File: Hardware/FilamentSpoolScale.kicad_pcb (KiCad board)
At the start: 2 copper layers, 62 x 76 mm, 7 parts, among them J1 0.91 inch OLED, J2 Load Cell, J3 Screw_Terminal_01x02, SW1 SW_Push

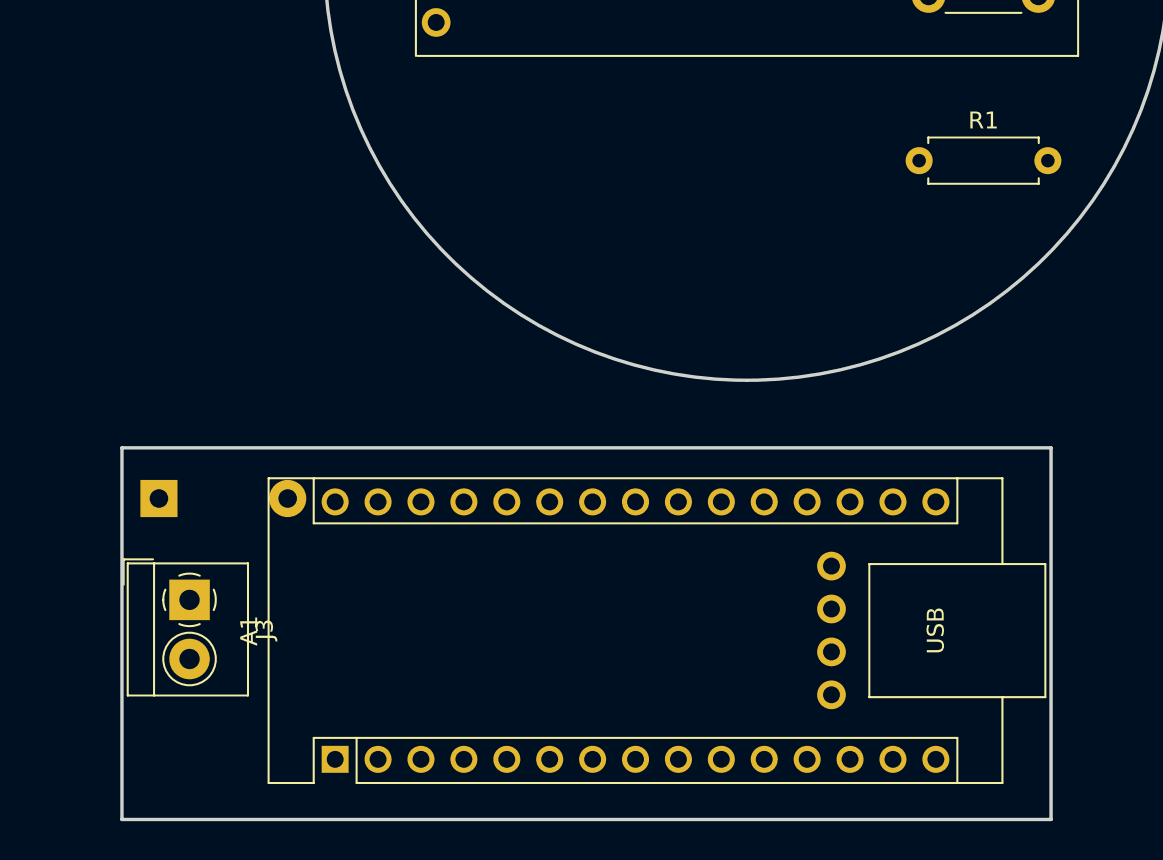
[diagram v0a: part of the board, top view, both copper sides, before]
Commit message: Addition of 2nd button (backup button)
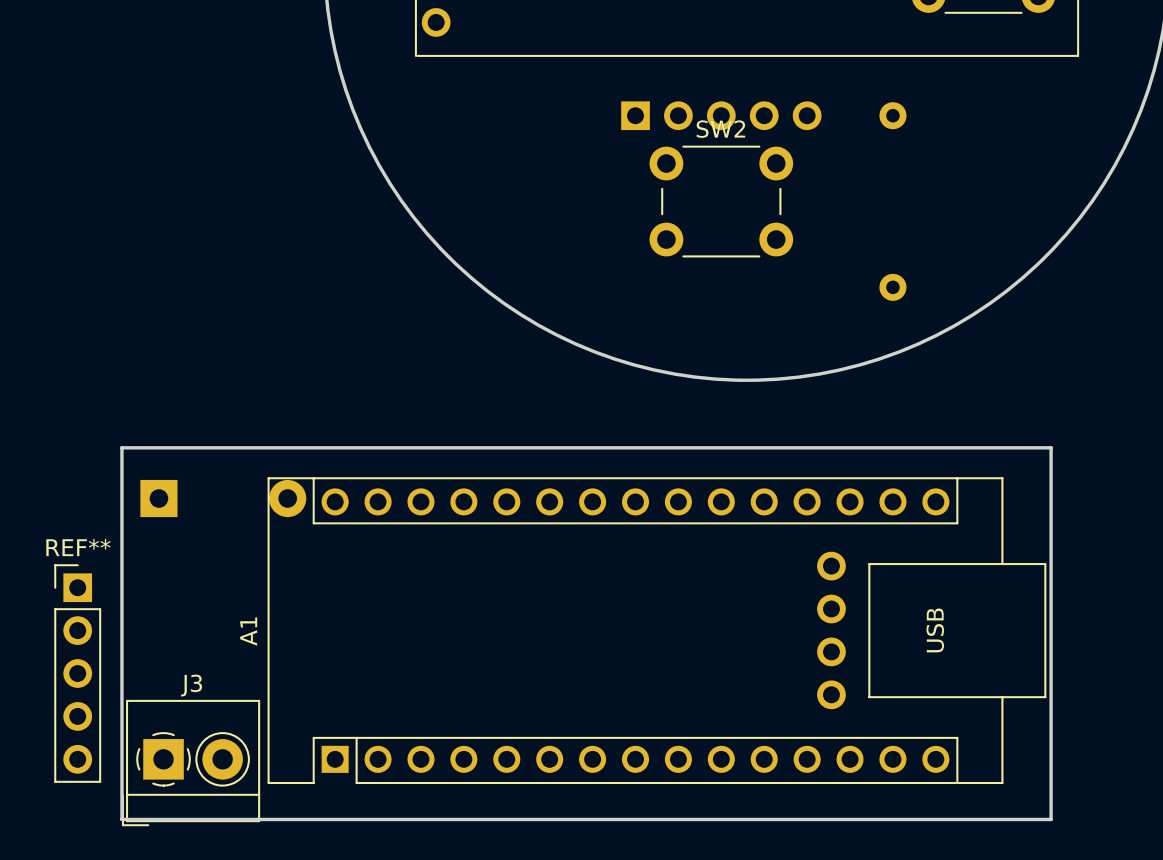
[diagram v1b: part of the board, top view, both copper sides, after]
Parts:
- added REF**: PinHeader_1x05_P2.54mm_Vertical, Connector_PinHeader_2.54mm:PinHeader_1x05_P2.54mm_Vertical, F.Cu at (119.4, 81.3)
- added REF**: PinHeader_1x05_P2.54mm_Horizontal, Connector_PinHeader_2.54mm:PinHeader_1x05_P2.54mm_Horizontal, B.Cu at (152.4, 53.3)
- added SW2: SW_Push, Button_Switch_THT:SW_PUSH_6mm_H4.3mm, F.Cu at (154.2, 56.2)
- R1: value 10k -> R; footprint Resistor_THT:R_Axial_DIN0207_L6.3mm_D2.5mm_P7.62mm_Horizontal -> Resistor_THT:R_Axial_DIN0207_L6.3mm_D2.5mm_P10.16mm_Horizontal; moved to B.Cu
- moved J3 9.56 mm to (124.5, 91.4), turned to 0 degrees
- moved R1 7.66 mm to (167.6, 63.5), turned to 90 degrees
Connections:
- A1 pad 1: unconnected-(A1-Pad1) -> /TX
- A1 pad 2: unconnected-(A1-Pad2) -> /RX
- A1 pad 5: /BT -> /BT1
- A1 pad 6: unconnected-(A1-Pad6) -> /BT2
- R1 pad 1: GND -> /BT2
- R1 pad 2: /BT -> GND
- SW1 pad 1: +5V -> /BT1
- SW1 pad 2: /BT -> GND

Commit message: Board design
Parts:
- removed REF**: PinHeader_1x05_P2.54mm_Vertical, Connector_PinHeader_2.54mm:PinHeader_1x05_P2.54mm_Vertical
- removed REF**: PinHeader_1x05_P2.54mm_Horizontal, Connector_PinHeader_2.54mm:PinHeader_1x05_P2.54mm_Horizontal
- added H1: MountingHole_Pad, MountingHole:MountingHole_3.2mm_M3_DIN965_Pad_TopBottom, F.Cu at (91.5, 33.5)
- added H2: MountingHole_Pad, MountingHole:MountingHole_3.2mm_M3_DIN965_Pad_TopBottom, F.Cu at (128.0, 33.5)
- added H3: MountingHole_Pad, MountingHole:MountingHole_3.2mm_M3_DIN965_Pad_TopBottom, F.Cu at (128.0, 61.5)
- added H4: MountingHole_Pad, MountingHole:MountingHole_3.2mm_M3_DIN965_Pad_TopBottom, F.Cu at (91.5, 61.5)
- added H5: MountingHole_Pad, MountingHole:MountingHole_3.2mm_M3_DIN965_Pad_TopBottom, F.Cu at (29.8, 38.0)
- added H6: MountingHole_Pad, MountingHole:MountingHole_3.2mm_M3_DIN965_Pad_TopBottom, F.Cu at (29.8, 57.0)
- added J4: Conn_01x03, Connector_PinHeader_2.54mm:PinHeader_1x03_P2.54mm_Vertical, F.Cu at (84.1, 62.4)
- added J5: Conn_01x06, Connector_PinHeader_2.54mm:PinHeader_1x06_P2.54mm_Vertical, F.Cu at (74.0, 41.1)
- added J6: Conn_01x06, Connector_PinHeader_2.54mm:PinHeader_1x06_P2.54mm_Horizontal, B.Cu at (36.2, 41.1)
- D1: moved to F.Cu
- J3: moved to B.Cu
- R1: value R -> 10k
- moved R1 129.1 mm to (38.9, 54.0), turned to -90 degrees
- moved SW1 127.5 mm to (44.5, 66.0), turned to 90 degrees
- moved SW2 123.0 mm to (31.8, 44.0), turned to -90 degrees
- moved J1 90.8 mm to (50.6, 27.9), turned to -90 degrees
- moved J3 73.1 mm to (78.4, 34.7)
- moved D1 57.5 mm to (86.3, 32.8), turned to -90 degrees
- moved A1 55.7 mm to (92.5, 55.0)
- moved J2 53.2 mm to (125.2, 43.5)
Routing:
- net +5V: track 0.00 -> 126.6 mm, vias 0 -> 2
- net /BT2: track 0.00 -> 102.1 mm, vias 0 -> 2
- net /SCL: track 0.00 -> 94.8 mm, vias 0 -> 3
- net /SDA: track 0.00 -> 92.8 mm, vias 0 -> 3
- net /BT1: track 0.00 -> 86.2 mm, vias 0 -> 2
- net /DT: track 0.00 -> 20.1 mm
- net GND: track 0.00 -> 19.7 mm, vias 0 -> 13
- net /SCK: track 0.00 -> 18.7 mm
- net /RX: track 0.00 -> 13.9 mm
- net /TX: track 0.00 -> 13.9 mm
- net BATT: track 0.00 -> 6.42 mm
- net Net-(D1-Pad1): track 0.00 -> 5.19 mm
- added copper zone on B.Cu, net GND
- added copper zone on F.Cu, net GND
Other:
- board size 62 x 76 mm -> 107.2 x 45 mm

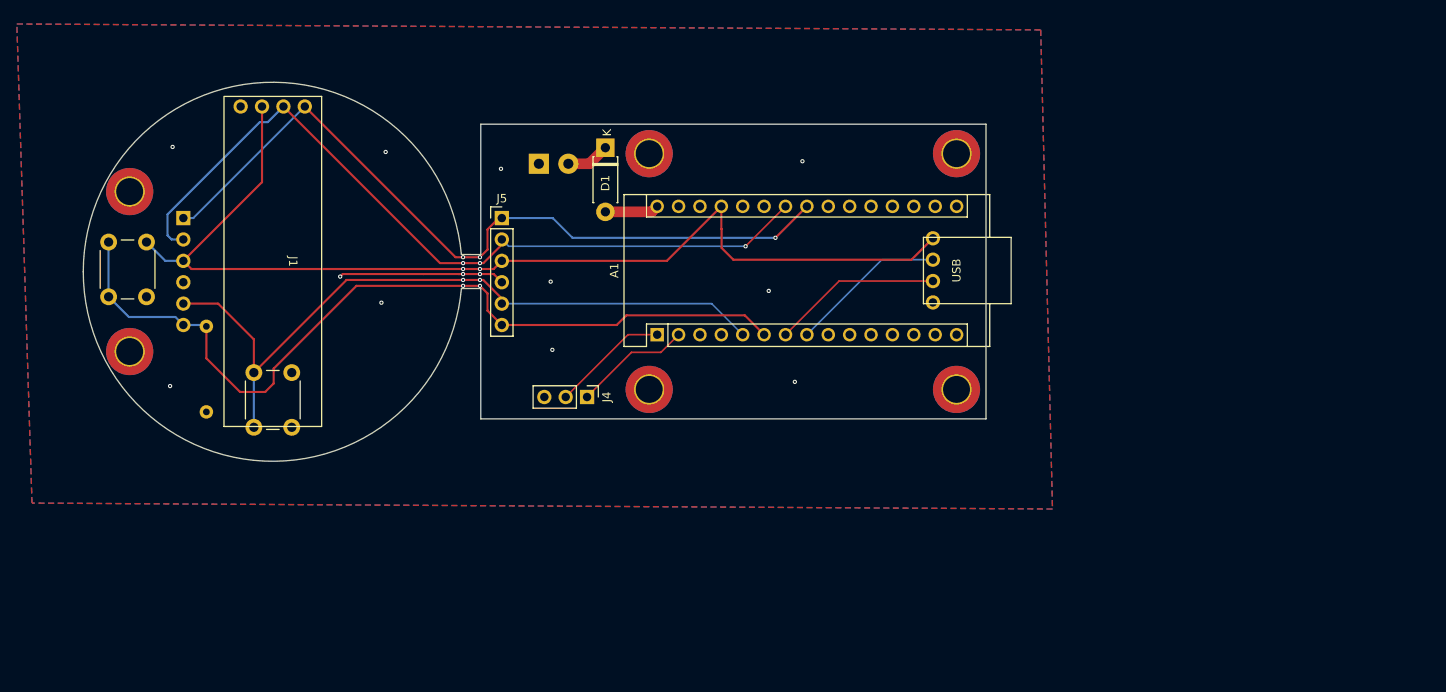
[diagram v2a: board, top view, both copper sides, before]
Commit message: Testing Software and hw changes
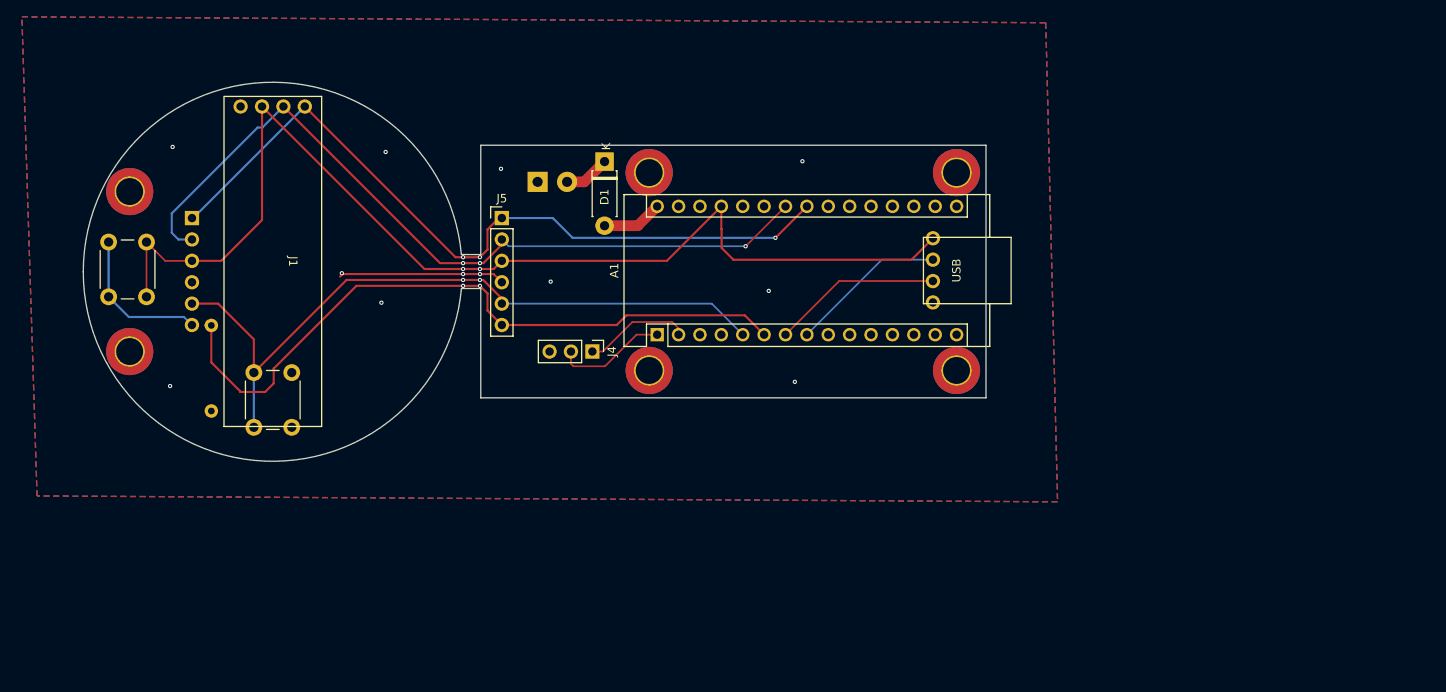
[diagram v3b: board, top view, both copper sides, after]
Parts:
- moved J4 5.44 mm to (84.8, 57.0)
- moved H1 2.25 mm to (91.5, 35.8)
- moved H2 2.25 mm to (128.0, 35.8)
- moved H3 2.25 mm to (128.0, 59.2)
- moved H4 2.25 mm to (91.5, 59.2)
- moved J3 2.16 mm to (78.2, 36.9)
- moved D1 1.65 mm to (86.2, 34.4)
- moved J6 1.03 mm to (37.2, 41.1)
- moved R1 0.60 mm to (39.5, 53.9)
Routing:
- net +5V: track 126.6 -> 133.9 mm
- net /BT2: track 102.1 -> 100.4 mm
- net /RX: track 13.9 -> 12.8 mm
- net /SDA: track 92.8 -> 91.8 mm
- net /BT1: track 86.2 -> 85.2 mm
- net BATT: track 6.42 -> 7.20 mm
- net /TX: track 13.9 -> 13.4 mm
- net GND: vias 13 -> 12
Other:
- outline, holes or cut-outs redrawn
